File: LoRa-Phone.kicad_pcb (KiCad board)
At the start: 6 copper layers, 60 x 105 mm, 245 parts, among them IC1 W9825G6KH-6I, J1 Conn_Coaxial, J10 GPIOs, J11 Micro_SD_Card, J3 USB-C, J4 BUTTON, J5 LED0123, J6 ROTARY_ENCODER, J7 3.3V, J8 AudioJack4_Ground_SwitchTR1, J9 SWD, M1 Motor_DC, Q2 AO3400A, Q3 AO3400A, Q4 2N7002, Q6 AO3401A, SW1 SW_Push, SW2 BOOT, SW3 RESET, U1 MAX16150AUT+T, U10 DRV2605LDGS, U11 LC76G, U13 SA818S, U14 74HC138, U15 STM32H743BITx, U17 TPS61165DRV, U18 CP2102N-Axx-xQFN24, U19 ESP32-C3-WROOM-02, U2 TPS62132, U21 WM8960, U22 TLV75528PDBV, U23 E22-900M30S, U24 E22-170M30S, U3 RV-3028-C7, U4 BMP390, U5 MAX98357A, U6 LSM6DSOXTR, U7 MAX17048G_T10, U8 BQ24072RGT, U9 PLP5012PWR, Y1 Crystal_GND24

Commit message: Routed RF Core
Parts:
- removed AE4, AE5: Antenna_Shield, Connector_Coaxial:SMA_Amphenol_132289_EdgeMount
- removed BT1: Battery_Cell, Connector_JST:JST_PH_S2B-PH-K_1x02_P2.00mm_Horizontal
- removed C10, C14, C82, C84: 0.1uF, Capacitor_SMD:C_0603_1608Metric
- removed C11: 3.3nF, Capacitor_SMD:C_0603_1608Metric
- removed C12 (x2): 100nF, Capacitor_SMD:C_0805_2012Metric
- removed C13: 22uF, Capacitor_SMD:C_0805_2012Metric
- removed C15, C41, C78: 10uF, Capacitor_SMD:C_0603_1608Metric
- removed C18, C19, C30, C31, C34, C60, C63, C64, C65, C66, C68, C70: 1uF, Capacitor_SMD:C_0603_1608Metric
- removed C20, C21, C22, C43, C44, C83, C85: 4.7uF, Capacitor_SMD:C_0603_1608Metric
- removed C32, C33, C71, C72, C73, C74, C75, C76, C77, C80, C81, C86: 100nF, Capacitor_SMD:C_0603_1608Metric
- removed C35 (x2): 10uF, Capacitor_SMD:C_0805_2012Metric
- removed C42: 220nF, Capacitor_SMD:C_0603_1608Metric
- removed C45, C46, C47, C48, C49, C50, C51, C52, C53, C54, C55, C56, C57, C58, C59, C67, C69, C79: 100nF, Capacitor_SMD:C_0402_1005Metric_Pad0.74x0.62mm_HandSolder
- removed the C6 at (277.0, 45.2)
- removed the C6 at (177.9, 82.1)
- removed C61, C62: 10uF, Capacitor_SMD:C_0402_1005Metric
- removed the C7 at (277.0, 47.7)
- removed the C7 at (177.9, 84.6)
- removed C88, C94: 12pF, Capacitor_SMD:C_0402_1005Metric
- removed C9: 10uF, Capacitor_SMD:C_1210_3225Metric
- removed D1: BAT54A, Package_TO_SOT_SMD:SOT-23
- removed D3: ~, Diode_SMD:D_SOD-123
- removed FB3, FB4: FerriteBead, Inductor_SMD:L_0805_2012Metric
- removed HOLE0 (x4): MountingHole_2.2mm_M2_DIN965_Pad, MountingHole:MountingHole_2.2mm_M2_DIN965_Pad
- removed J10: GPIOs, Connector_PinHeader_2.54mm:PinHeader_2x17_P2.54mm_Vertical
- removed J11: Micro_SD_Card, PTCR:J_SD_Card-micro_socket_A
- removed J3: USB-C, Connector_USB:USB_C_Receptacle_GCT_USB4105-xx-A_16P_TopMnt_Horizontal
- removed J5: LED0123, Connector_PinHeader_1.27mm:PinHeader_2x06_P1.27mm_Vertical
- removed J7: 3.3V, Connector_PinHeader_1.27mm:PinHeader_1x01_P1.27mm_Vertical
- removed J8: AudioJack4_Ground_SwitchTR1, Connector_Audio:Jack_3.5mm_PJ31060-I_Horizontal
- removed J9: SWD, Connector_PinHeader_2.54mm:PinHeader_1x05_P2.54mm_Vertical
- removed L1: 2.2uH, Inductor_SMD:L_Coilcraft_XxL4020
- removed L3: 10uH, Inductor_SMD:L_Bourns-SRN4018
- removed LS1: Speaker, Connector_PinHeader_1.27mm:PinHeader_1x02_P1.27mm_Vertical
- removed MK1: ICS-43434, Connector_PinHeader_1.27mm:PinHeader_2x03_P1.27mm_Vertical
- removed Q2, Q3: AO3400A, Package_TO_SOT_SMD:SOT-23
- removed Q4: 2N7002, Package_TO_SOT_SMD:SOT-23
- removed Q6: AO3401A, Package_TO_SOT_SMD:SOT-23
- removed R10, R12, R13, R17, R18, R19, R59, R60, R62: 100K, Resistor_SMD:R_0603_1608Metric
- removed R14, R23, R27, R32, R35, R37, R38, R61, R63, R64, R69, R71, R72, R73, R9: 10K, Resistor_SMD:R_0603_1608Metric
- removed R20: 46.4K, Resistor_SMD:R_0603_1608Metric
- removed R21: 1.18K, Resistor_SMD:R_0603_1608Metric
- removed R22: 1.13K, Resistor_SMD:R_0603_1608Metric
- removed R25: 5K, Resistor_SMD:R_0603_1608Metric
- removed R26, R28: 1.5K, Resistor_SMD:R_0603_1608Metric
- removed R29, R30: 5.1K, Resistor_SMD:R_0603_1608Metric
- removed R31 (x2), R65 (x2), R66 (x2), R67 (x2), R68 (x2): 47K, Resistor_SMD:R_0603_1608Metric_Pad0.98x0.95mm_HandSolder
- removed R33, R34: 4.7K, Resistor_SMD:R_0603_1608Metric
- removed R36: 0.57R, Resistor_SMD:R_0603_1608Metric
- removed R39, R40, R41, R42, R43, R44, R45, R46, R47, R48, R49, R50, R51, R52, R53, R54, R55, R56, R57, R58: 22R, Resistor_SMD:R_0402_1005Metric
- removed SW1: SW_Push, Connector_PinHeader_1.27mm:PinHeader_1x02_P1.27mm_Vertical
- removed SW2: BOOT, Button_Switch_SMD:Panasonic_EVQPUJ_EVQPUA
- removed SW3: RESET, Button_Switch_SMD:Panasonic_EVQPUJ_EVQPUA
- removed TP1: +BATT, TestPoint:TestPoint_Pad_D1.0mm
- removed TP3: GND, TestPoint:TestPoint_Pad_D1.0mm
- removed TP5: CLR, TestPoint:TestPoint_Pad_D1.0mm
- removed TP6: 3V3, TestPoint:TestPoint_Pad_D1.0mm
- removed TP7: VBUS, TestPoint:TestPoint_Pad_D1.0mm
- removed TP8: CHG, TestPoint:TestPoint_Pad_D1.0mm
- removed TP9: VCC, TestPoint:TestPoint_Pad_D1.0mm
- removed U14: 74HC138, PTCR:SO-16
- removed U15: STM32H743BITx, Package_QFP:LQFP-208_28x28mm_P0.5mm
- removed U16: ~, Connector_FFC-FPC:TE_4-1734839-0_1x40-1MP_P0.5mm_Horizontal
- removed U17: TPS61165DRV, Package_SON:WSON-6-1EP_2x2mm_P0.65mm_EP1x1.6mm
- removed U18: CP2102N-Axx-xQFN24, Package_DFN_QFN:QFN-24-1EP_4x4mm_P0.5mm_EP2.6x2.6mm
- removed U19: ESP32-C3-WROOM-02, RF_Module:ESP32-C3-WROOM-02U
- removed U20: ~, Connector_FFC-FPC:TE_2-1734839-4_1x24-1MP_P0.5mm_Horizontal
- removed U22: TLV75528PDBV, Package_TO_SOT_SMD:SOT-23-5
- removed U5: MAX98357A, PTCR:QFN50P300X300X100-17N-D
- removed U7: MAX17048G_T10, PTCR:SON50P200X200X80-9N-R100X170
- removed U8: BQ24072RGT, PTCR:QFN50P300X300X100-17N-D
- removed U9: PLP5012PWR, PTCR:TSSOP24_PW_TEX
- removed Y1: Crystal_GND24, Crystal:Crystal_SMD_Abracon_ABM8AIG-4Pin_3.2x2.5mm
- added C100: 100pF, Capacitor_SMD:C_0603_1608Metric, F.Cu at (383.2, 65.6)
- added C101: 1nF, Capacitor_SMD:C_0402_1005Metric, F.Cu at (173.2, 64.9)
- added C102: 1nF, Capacitor_SMD:C_0402_1005Metric, F.Cu at (172.7, 60.9)
- added C103: 1nF, Capacitor_SMD:C_0402_1005Metric, F.Cu at (191.0, 76.9)
- added C104: 100pF, Capacitor_SMD:C_0603_1608Metric, F.Cu at (383.2, 75.7)
- added C105: 0.1uF, Capacitor_SMD:C_0603_1608Metric, F.Cu at (383.2, 78.2)
- added C106: 100pF, Capacitor_SMD:C_0603_1608Metric, F.Cu at (383.2, 80.7)
- added C107: 0.1uF, Capacitor_SMD:C_0603_1608Metric, F.Cu at (383.2, 83.2)
- added C108: 1nF, Capacitor_SMD:C_0603_1608Metric, F.Cu at (387.2, 63.1)
- added C109: 100pF, Capacitor_SMD:C_0603_1608Metric, F.Cu at (387.2, 65.6)
- added C110: 0.1uF, Capacitor_SMD:C_0603_1608Metric, F.Cu at (387.2, 68.1)
- added C111: 1nF, Capacitor_SMD:C_0603_1608Metric, F.Cu at (387.2, 70.7)
- added C112: 1nF, Capacitor_SMD:C_0402_1005Metric, F.Cu at (387.2, 73.2)
- added C113: 100pF, Capacitor_SMD:C_0603_1608Metric, F.Cu at (387.2, 75.7)
- added C114: 0.1uF, Capacitor_SMD:C_0603_1608Metric, F.Cu at (387.2, 78.2)
- added C6: 100nF, Capacitor_SMD:C_0603_1608Metric, F.Cu at (371.1, 68.1)
- added C7: 10uF, Capacitor_SMD:C_0603_1608Metric, F.Cu at (371.1, 70.7)
- added C99: 100pF, Capacitor_SMD:C_0603_1608Metric, F.Cu at (383.2, 63.1)
- added IC2: AD8318ACPZ-REEL7, PTCR:QFN65P400X400X100-17N, F.Cu at (184.3, 57.3)
- added IC3: AD8318ACPZ-REEL7, PTCR:QFN65P400X400X100-17N, F.Cu at (183.1, 67.0)
- added MH0: MountingHole_2.2mm_M2_DIN965_Pad_TopBottom, MountingHole:MountingHole_2.2mm_M2_DIN965_Pad_TopBottom, F.Cu at (171.6, 56.5)
- added MH0: MountingHole_2.2mm_M2_DIN965_Pad_TopBottom, MountingHole:MountingHole_2.2mm_M2_DIN965_Pad_TopBottom, F.Cu at (121.6, 56.5)
- added MH0: MountingHole_2.2mm_M2_DIN965_Pad_TopBottom, MountingHole:MountingHole_2.2mm_M2_DIN965_Pad_TopBottom, F.Cu at (121.6, 148.5)
- added R84: 96.2R, Resistor_SMD:R_0402_1005Metric, F.Cu at (137.3, 64.5)
- added R85: 71.5R, Resistor_SMD:R_0402_1005Metric, F.Cu at (135.5, 64.0)
- added R86: 96.2R, Resistor_SMD:R_0402_1005Metric, F.Cu at (133.9, 60.3)
- added R87: 96.2R, Resistor_SMD:R_0402_1005Metric, F.Cu at (137.3, 60.3)
- added R88: 71.5R, Resistor_SMD:R_0402_1005Metric, F.Cu at (135.5, 60.8)
- added R89: 52.3R, Resistor_SMD:R_0402_1005Metric, F.Cu at (392.4, 129.6)
- added R90: 499R, Resistor_SMD:R_0402_1005Metric, F.Cu at (392.4, 131.6)
- added R91: 10K, Resistor_SMD:R_0402_1005Metric, F.Cu at (392.4, 133.6)
- added R92: 10K, Resistor_SMD:R_0402_1005Metric, F.Cu at (392.4, 135.5)
- added R93: 52.3R, Resistor_SMD:R_0402_1005Metric, F.Cu at (395.3, 127.6)
- added R94: 499R, Resistor_SMD:R_0402_1005Metric, F.Cu at (395.3, 129.6)
- added R95: 10K, Resistor_SMD:R_0603_1608Metric, F.Cu at (391.2, 83.2)
- added R96: 1K, Resistor_SMD:R_0402_1005Metric, F.Cu at (395.3, 131.6)
- added R97: 1K, Resistor_SMD:R_0402_1005Metric, F.Cu at (395.3, 133.6)
- AE1: value Antenna_Shield -> GNSS
- AE6: value Antenna_Shield -> SMA; moved to F.Cu
- IC1: value W9825G6KH-6I -> SKY13373-460LF; footprint PTCR:SOP80P1176X120-54N -> PTCR:QFN50P200X200X60-13N-D
- J1: value Conn_Coaxial -> Interface; footprint Connector_Coaxial:U.FL_Molex_MCRF_73412-0110_Vertical -> Connector_PinHeader_2.54mm:PinHeader_2x20_P2.54mm_Vertical; moved to B.Cu
- R83: value 1M -> 96.2R
- U1: value MAX16150AUT+T -> ESP32-S3-WROOM-2; footprint PTCR:21-0058I_MXM -> RF_Module:ESP32-S3-WROOM-2
- U11, U23: moved to F.Cu
- U2: value TPS62132 -> TCD-10-23BDX+; footprint PTCR:RGT16_1P7X1P7 -> PTCR:TCD-10-23BDX+
- U3: value RV-3028-C7 -> MCP23017x-x-ML; footprint Package_SON:MicroCrystal_C7_SON-8_1.5x3.2mm_P0.9mm -> Package_DFN_QFN:QFN-28-1EP_6x6mm_P0.65mm_EP4.25x4.25mm
- moved U21 245.2 mm to (391.4, 140.0)
- moved C40 203.9 mm to (379.1, 63.1)
- moved C95 202.6 mm to (379.1, 80.7)
- moved C96 202.6 mm to (379.1, 83.2)
- moved C23 196.7 mm to (371.1, 80.7)
- moved C36 195.4 mm to (375.1, 75.7)
- moved C37 195.4 mm to (375.1, 78.2)
- moved C38 195.4 mm to (375.1, 80.7)
- moved C39 195.4 mm to (375.1, 83.2)
- moved C16 194.7 mm to (371.1, 75.7)
- moved C17 194.7 mm to (371.1, 78.2)
- moved C25 193.9 mm to (375.1, 63.1)
- moved C26 193.9 mm to (375.1, 65.6)
- moved C27 193.9 mm to (375.1, 68.1)
- moved C28 193.9 mm to (375.1, 70.7)
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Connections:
- AE6 pad 1: Net-(AE6-A) -> ANT
- C25 pad 1: NRST_900 -> NRST_RADIO
- C28 pad 1: NRST_170 -> NRST_RADIO
- C4 pad 2: +2V8 -> +3V3
- C8 pad 1: CLR_POWER -> +3V3
- IC1 pad 1: +3V3 -> RF1
- IC1 pad 10: DQ5 -> GND
- IC1 pad 11: DQ6 -> ROS
- IC1 pad 13: DQ7 -> GND
- IC1 pad 2: DQ0 -> GND
- IC1 pad 3: +3V3 -> RF3
- IC1 pad 4: DQ1 -> RFS_V1
- IC1 pad 5: DQ2 -> RFS_V2
- IC1 pad 6: GND -> +3V3
- IC1 pad 7: DQ3 -> GND
- IC1 pad 8: DQ4 -> GND
- IC1 pad 9: +3V3 -> RF2
- J1 pad 1: unconnected-(J1-In-Pad1) -> +5V
- J1 pad 2: GND -> +3V3
- R81 pad 2: Net-(U15-PA2) -> Net-(U1-IO38)
- R82 pad 2: Net-(U15-PA3) -> Net-(U1-MTCK/IO39)
- R83 pad 1: XTAL2 -> FWD_IN
- R83 pad 2: XTAL1 -> GND
- U1 pad 1: Net-(U1-*PB_IN) -> GND
- U1 pad 2: GND -> +3V3
- U1 pad 3: VCC -> S3_EN
- U1 pad 4: EN_POWER -> FWD
- U1 pad 5: unconnected-(U1-*INT-Pad5) -> BUSY_170
- U1 pad 6: CLR_POWER -> DIO1_900
- U11 pad 4: 1PPS -> unconnected-(U11-1PPS-Pad4)
- U13 pad 12: Net-(AE5-A) -> RF1
- U2 pad 1: Net-(L1-Pad2) -> FWD_IN
- U2 pad 2: Net-(L1-Pad2) -> GND
- U2 pad 3: Net-(L1-Pad2) -> ROS
- U2 pad 4: Net-(U2-PG) -> ANT
- U2 pad 6: GND -> REV_IN
- U21 pad 17: WM8960_SCL -> SCL
- U21 pad 18: WM8960_SDA -> SDA
- U23 pad 15: NRST_900 -> NRST_RADIO
- U23 pad 21: Net-(AE6-A) -> RF2
- U23 pad 7: TXEN_900 -> Net-(U23-DIO2)
- U23 pad 8: DIO2_900 -> Net-(U23-DIO2)
- U24 pad 15: NRST_170 -> NRST_RADIO
- U24 pad 21: Net-(AE4-A) -> RF3
- U24 pad 7: TXEN_170 -> Net-(U24-DIO2)
- U24 pad 8: DIO2_170 -> Net-(U24-DIO2)
- U3 pad 1: unconnected-(U3-CLKOUT-Pad1) -> MOTOR
- U3 pad 2: INT_RTC -> RXEN_170
- U3 pad 3: SCL -> NRST_RADIO
- U3 pad 4: SDA -> RXEN_900
- U3 pad 5: GND -> +3V3
- U3 pad 6: +BATT -> GND
- U3 pad 7: +3V3 -> unconnected-(U3-NC-Pad7)
- U3 pad 8: unconnected-(U3-EVI-Pad8) -> SCL
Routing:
- net A10: track 57.9 -> 0.00 mm, vias 2 -> 0
- net ~CS: track 49.9 -> 0.00 mm, vias 2 -> 0
- net A11: track 48.7 -> 0.00 mm, vias 2 -> 0
- net Net-(C45-Pad1): track 46.6 -> 0.00 mm
- net A9: track 45.8 -> 0.00 mm, vias 2 -> 0
- net A8: track 44.7 -> 0.00 mm, vias 2 -> 0
- net CKE: track 44.5 -> 0.00 mm, vias 2 -> 0
- net A5: track 44.0 -> 0.00 mm
- net A7: track 43.4 -> 0.00 mm, vias 2 -> 0
- net A6: track 43.1 -> 0.00 mm, vias 2 -> 0
- net A4: track 42.7 -> 0.00 mm
- net A3: track 40.9 -> 0.00 mm, vias 2 -> 0
- net A2: track 40.9 -> 0.00 mm, vias 2 -> 0
- net A12: track 40.4 -> 0.00 mm, vias 2 -> 0
- net A1: track 40.2 -> 0.00 mm, vias 2 -> 0
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- added copper zone on F.Cu, net RF2
- added copper zone on F.Cu, net RF3
- added copper zone on F.Cu, net ROS
- removed copper zone on F.Cu, net +3V3
- removed copper zone on F.Cu, net +BATT
- removed copper zone on In3.Cu, net GND
- removed copper zone on In4.Cu, net GND
- removed copper zone on B.Cu, net VBUS
- removed copper zone on F.Cu, net VBUS
- removed copper zone on F.Cu, net VCC
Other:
- board size 60 x 105 mm -> 60 x 102.5 mm
- copper layers 6 -> 4

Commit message: Routed RF part and started routing MCU, SPI Bus, and other
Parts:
- removed C17, C36: 4.7uF, Capacitor_SMD:C_0603_1608Metric
- removed R91: 10K, Resistor_SMD:R_0402_1005Metric
- added REF**: antipad, PTCR:antipad, F.Cu at (122.5, 70.1)
- C104, C105, C106, C107, C108, C109, C110, C111, C113, C114: footprint Capacitor_SMD:C_0603_1608Metric -> Capacitor_SMD:C_0402_1005Metric
- moved C37 308.6 mm to (66.7, 68.9)
- moved R74 308.6 mm to (78.7, 74.0)
- moved R75 308.6 mm to (82.7, 53.9)
- moved R76 308.6 mm to (82.7, 56.4)
- moved R77 308.6 mm to (82.7, 58.9)
- moved C87 308.6 mm to (70.7, 56.4)
- moved C89 308.6 mm to (70.7, 58.9)
- moved C90 308.6 mm to (70.7, 61.4)
- moved C92 308.6 mm to (70.7, 66.4)
- moved C93 308.6 mm to (70.7, 68.9)
- moved R93 262.2 mm to (142.9, 56.5), turned to -90 degrees
- moved R89 257.6 mm to (142.5, 66.9), turned to 90 degrees
- moved R94 257.4 mm to (149.2, 54.1), turned to 90 degrees
- moved R97 254.0 mm to (152.7, 58.0), turned to 180 degrees
- moved R90 252.8 mm to (148.8, 63.7), turned to 90 degrees
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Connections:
- C16 pad 1: Net-(U21-AVDD) -> +3V3
- C38 pad 1: Net-(U21-DCVDD) -> +3V3
- U21 pad 21: Net-(U21-SPKVDD2) -> unconnected-(U21-SPKVDD2-Pad21)
- U21 pad 26: Net-(U21-SPKVDD1) -> unconnected-(U21-SPKVDD1-Pad26)
- U21 pad 32: Net-(U21-AVDD) -> +3V3
- U21 pad 8: Net-(U21-DCVDD) -> +3V3
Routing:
- net MOSI: track 0.00 -> 124.2 mm, vias 0 -> 6
- net CLK: track 0.00 -> 119.4 mm, vias 0 -> 6
- net MISO: track 0.00 -> 117.2 mm, vias 0 -> 4
- net +3V3: track 0.00 -> 96.7 mm, vias 0 -> 6
- net FWD: track 0.00 -> 96.5 mm, vias 0 -> 2
- net DIO1_900: track 0.00 -> 94.6 mm, vias 0 -> 4
- net CS_900: track 0.00 -> 88.3 mm, vias 0 -> 4
- net REV: track 0.00 -> 82.8 mm, vias 0 -> 2
- net PTT: track 0.00 -> 79.9 mm, vias 0 -> 5
- net BUSY_900: track 0.00 -> 75.6 mm, vias 0 -> 4
- net NRST_RADIO: track 0.00 -> 69.1 mm, vias 0 -> 3
- net CS_170: track 0.00 -> 59.1 mm, vias 0 -> 3
- net BUSY_170: track 0.99 -> 58.1 mm, vias 0 -> 2
- net H/L: track 0.00 -> 56.0 mm, vias 0 -> 3
- net MONO_OUT: track 0.00 -> 52.2 mm, vias 0 -> 1
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- added copper zone on F.Cu, net +3V3
- added copper zone on In2.Cu, net +3V3
- added copper zone on F.Cu, net RF1
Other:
- outline, holes or cut-outs redrawn

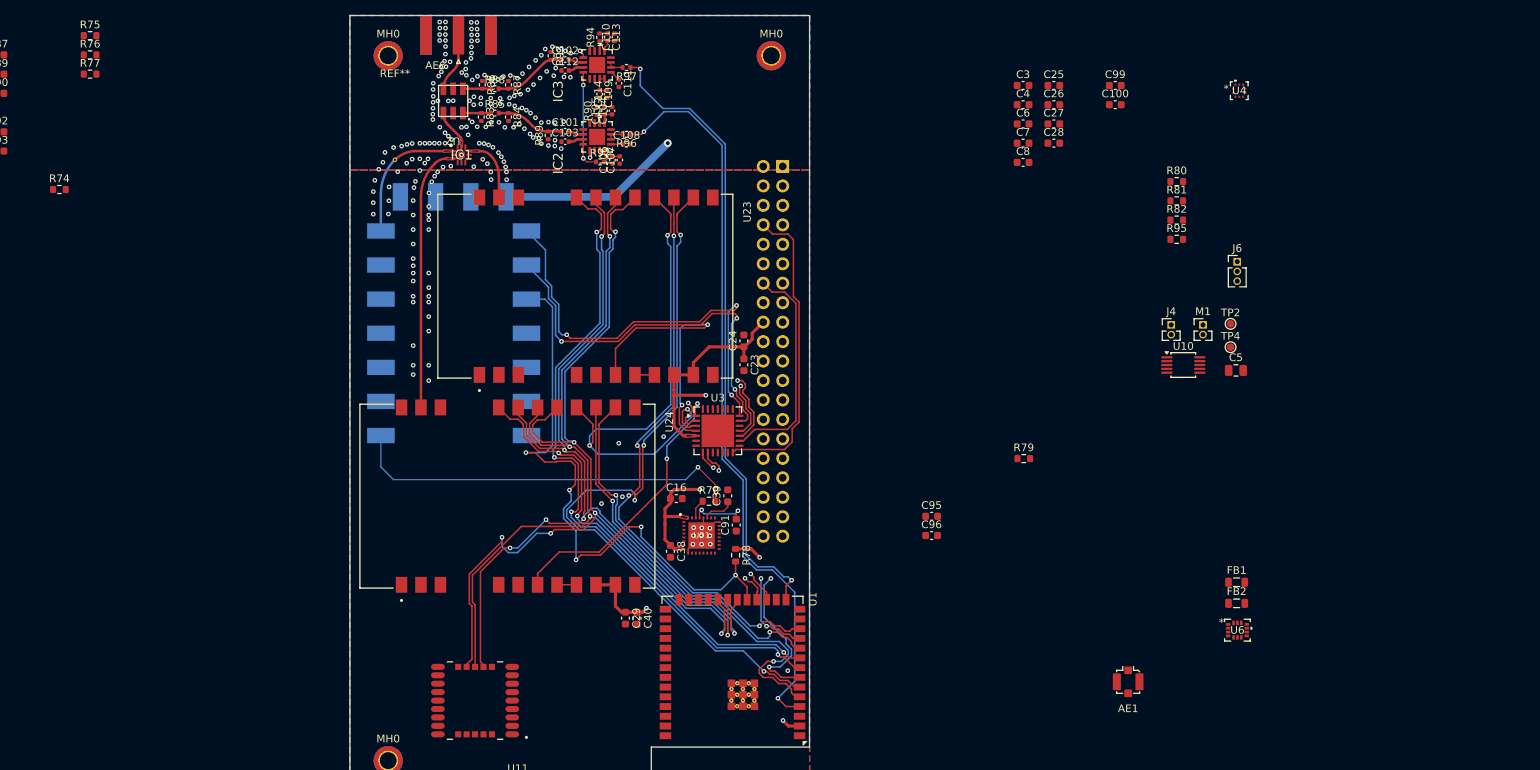
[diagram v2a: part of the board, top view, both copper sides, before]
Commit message: Modified schematic to add dual battery with dual charger, dual gauge and power mux
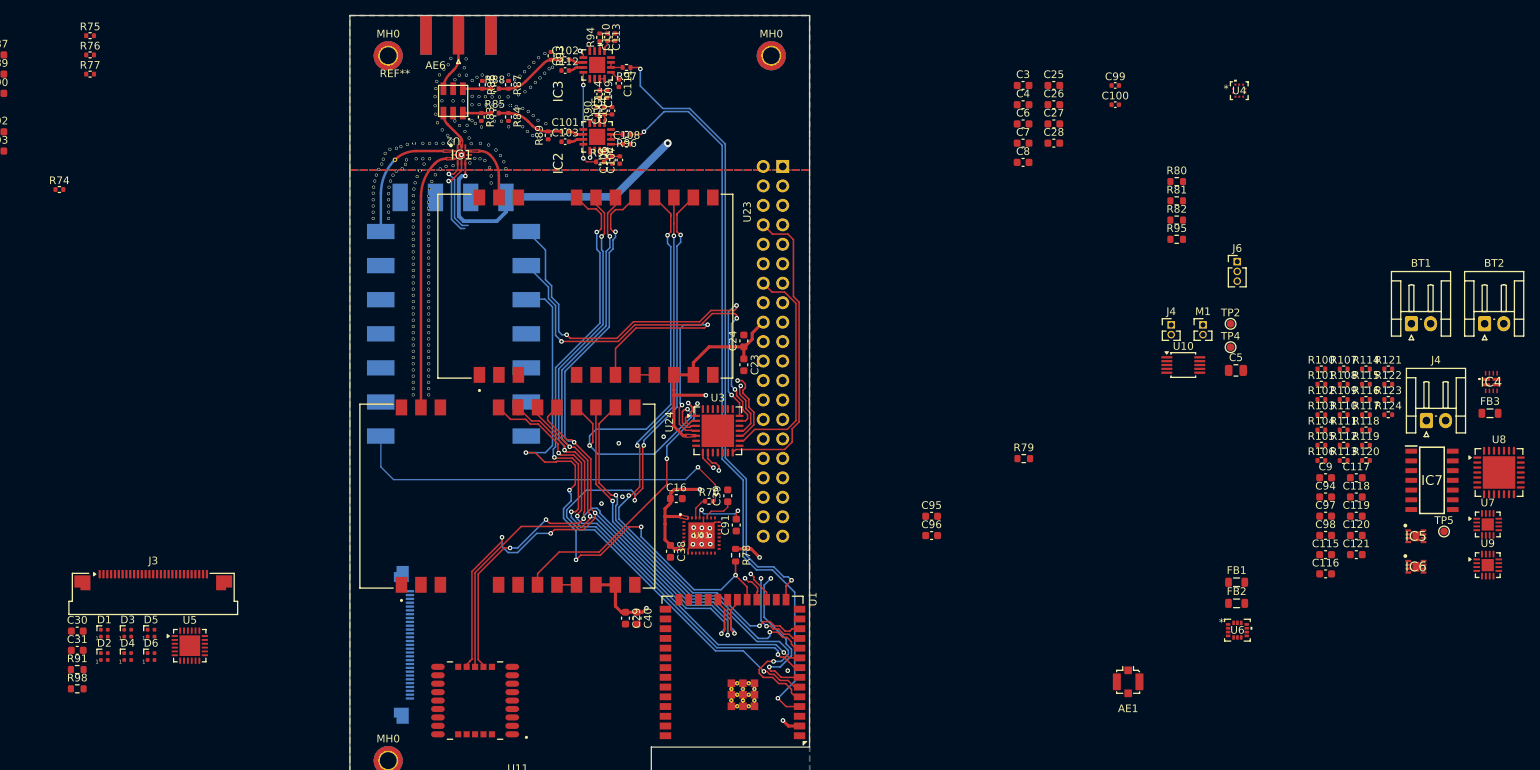
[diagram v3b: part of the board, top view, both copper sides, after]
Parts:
- added BT1: MAIN, Connector_JST:JST_EH_S2B-EH_1x02_P2.50mm_Horizontal, F.Cu at (255.2, 91.5)
- added BT2: SECOND, Connector_JST:JST_EH_S2B-EH_1x02_P2.50mm_Horizontal, F.Cu at (264.7, 91.5)
- added C115: 4.7uF, Capacitor_SMD:C_0603_1608Metric, F.Cu at (243.9, 121.6)
- added C116: 1uF, Capacitor_SMD:C_0603_1608Metric, F.Cu at (243.9, 124.1)
- added C117: 1uF, Capacitor_SMD:C_0603_1608Metric, F.Cu at (248.0, 111.6)
- added C118: 1uF, Capacitor_SMD:C_0603_1608Metric, F.Cu at (248.0, 114.1)
- added C119: 4.7uF, Capacitor_SMD:C_0603_1608Metric, F.Cu at (248.0, 116.6)
- added C120: 4.7uF, Capacitor_SMD:C_0603_1608Metric, F.Cu at (248.0, 119.1)
- added C121: 100nF, Capacitor_SMD:C_0603_1608Metric, F.Cu at (248.0, 121.6)
- added C30: 1uF, Capacitor_SMD:C_0603_1608Metric, F.Cu at (81.0, 131.6)
- added C31: 0.1uF, Capacitor_SMD:C_0603_1608Metric, F.Cu at (81.0, 134.1)
- added C9: 100nF, Capacitor_SMD:C_0603_1608Metric, F.Cu at (243.9, 111.6)
- added C94: 0.1uF, Capacitor_SMD:C_0603_1608Metric, F.Cu at (243.9, 114.1)
- added C97: 4.7uF, Capacitor_SMD:C_0603_1608Metric, F.Cu at (243.9, 116.6)
- added C98: 1uF, Capacitor_SMD:C_0603_1608Metric, F.Cu at (243.9, 119.1)
- added D1: LED_ARBG, LED_SMD:LED_SK6812_EC15_1.5x1.5mm, F.Cu at (84.5, 131.9)
- added D2: LED_ARBG, LED_SMD:LED_SK6812_EC15_1.5x1.5mm, F.Cu at (84.5, 134.9)
- added D3: LED_ARBG, LED_SMD:LED_SK6812_EC15_1.5x1.5mm, F.Cu at (87.6, 131.9)
- added D4: LED_ARBG, LED_SMD:LED_SK6812_EC15_1.5x1.5mm, F.Cu at (87.6, 134.9)
- added D5: LED_ARBG, LED_SMD:LED_SK6812_EC15_1.5x1.5mm, F.Cu at (90.7, 131.9)
- added D6: LED_ARBG, LED_SMD:LED_SK6812_EC15_1.5x1.5mm, F.Cu at (90.7, 134.9)
- added FB3: FerriteBead, Inductor_SMD:L_0805_2012Metric, F.Cu at (265.4, 103.2)
- added IC4: TPS2121RUXT, PTCR:TPS2121RUXT, F.Cu at (265.6, 99.1)
- added IC5: MAX17048G+T10, PTCR:SON50P200X200X80-9N-D, F.Cu at (255.7, 119.2)
- added IC6: MAX17048G+T10, PTCR:SON50P200X200X80-9N-D, F.Cu at (255.7, 123.2)
- added IC7: TCA9543ADR, PTCR:SOIC127P600X175-14N, F.Cu at (257.8, 111.9)
- added J2: Connector, Connector_FFC-FPC:Amphenol_F32R-1A7x1-11029_1x29-1MP_P0.5mm_Horizontal, B.Cu at (121.5, 133.4)
- added J3: Connector, Connector_FFC-FPC:Amphenol_F32R-1A7x1-11029_1x29-1MP_P0.5mm_Horizontal, F.Cu at (90.9, 127.1)
- added J4: JST_MAIN, Connector_JST:JST_EH_S2B-EH_1x02_P2.50mm_Horizontal, F.Cu at (257.1, 104.1)
- added R100: 13.7K, Resistor_SMD:R_0402_1005Metric, F.Cu at (243.4, 97.4)
- added R101: 23.7K, Resistor_SMD:R_0402_1005Metric, F.Cu at (243.4, 99.4)
- added R102: 5K, Resistor_SMD:R_0402_1005Metric, F.Cu at (243.4, 101.4)
- added R103: 5K, Resistor_SMD:R_0402_1005Metric, F.Cu at (243.4, 103.4)
- added R104: 51.1K, Resistor_SMD:R_0402_1005Metric, F.Cu at (243.4, 105.3)
- added R105: 10.2K, Resistor_SMD:R_0402_1005Metric, F.Cu at (243.4, 107.3)
- added R106: 5K, Resistor_SMD:R_0402_1005Metric, F.Cu at (243.4, 109.3)
- added R107: 1K, Resistor_SMD:R_0402_1005Metric, F.Cu at (246.3, 97.4)
- added R108: 1K, Resistor_SMD:R_0402_1005Metric, F.Cu at (246.3, 99.4)
- added R109: 10K, Resistor_SMD:R_0402_1005Metric, F.Cu at (246.3, 101.4)
- added R110: 1.13K, Resistor_SMD:R_0402_1005Metric, F.Cu at (246.3, 103.4)
- added R111: 1.18K, Resistor_SMD:R_0402_1005Metric, F.Cu at (246.3, 105.3)
- added R112: 1.18K, Resistor_SMD:R_0402_1005Metric, F.Cu at (246.3, 107.3)
- added R113: 1.13K, Resistor_SMD:R_0402_1005Metric, F.Cu at (246.3, 109.3)
- added R114: 1K, Resistor_SMD:R_0402_1005Metric, F.Cu at (249.2, 97.4)
- added R115: 1K, Resistor_SMD:R_0402_1005Metric, F.Cu at (249.2, 99.4)
- added R116: 10K, Resistor_SMD:R_0402_1005Metric, F.Cu at (249.2, 101.4)
- added R117: 10K, Resistor_SMD:R_0402_1005Metric, F.Cu at (249.2, 103.4)
- added R118: 10K, Resistor_SMD:R_0402_1005Metric, F.Cu at (249.2, 105.3)
- added R119: 10K, Resistor_SMD:R_0402_1005Metric, F.Cu at (249.2, 107.3)
- added R120: 10K, Resistor_SMD:R_0402_1005Metric, F.Cu at (249.2, 109.3)
- added R121: 10K, Resistor_SMD:R_0402_1005Metric, F.Cu at (252.1, 97.4)
- added R122: 10K, Resistor_SMD:R_0402_1005Metric, F.Cu at (252.1, 99.4)
- added R123: 10K, Resistor_SMD:R_0402_1005Metric, F.Cu at (252.1, 101.4)
- added R124: 10K, Resistor_SMD:R_0402_1005Metric, F.Cu at (252.1, 103.4)
- added R91: 3.3K, Resistor_SMD:R_0603_1608Metric, F.Cu at (81.0, 136.6)
- added R98: 10K, Resistor_SMD:R_0603_1608Metric, F.Cu at (81.0, 139.1)
- added TP5: +3V3_RF, TestPoint:TestPoint_Pad_D1.0mm, F.Cu at (259.4, 118.6)
- added U5: IS31FL3218-QF, Package_DFN_QFN:QFN-24-1EP_4x4mm_P0.5mm_EP2.7x2.7mm, F.Cu at (95.7, 133.5)
- added U7: BQ24075RGT, Package_DFN_QFN:VQFN-16-1EP_3x3mm_P0.5mm_EP1.6x1.6mm, F.Cu at (265.1, 117.7)
- added U8: MCP23017x-x-ML, Package_DFN_QFN:QFN-28-1EP_6x6mm_P0.65mm_EP4.25x4.25mm, F.Cu at (266.6, 110.9)
- added U9: BQ24075RGT, Package_DFN_QFN:VQFN-16-1EP_3x3mm_P0.5mm_EP1.6x1.6mm, F.Cu at (265.1, 123.0)
- C100, C99: footprint Capacitor_SMD:C_0603_1608Metric -> Capacitor_SMD:C_0402_1005Metric
- R70, R74, R75, R76, R77: footprint Resistor_SMD:R_0603_1608Metric -> Resistor_SMD:R_0402_1005Metric
- moved U13 0.07 mm to (130.1, 92.8)
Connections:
- C104 pad 1: +3V3 -> +3V3_RF
- C105 pad 1: +3V3 -> +3V3_RF
- C106 pad 2: +3V3 -> +3V3_RF
- C107 pad 2: +3V3 -> +3V3_RF
- C109 pad 1: +3V3 -> +3V3_RF
- C110 pad 1: +3V3 -> +3V3_RF
- C113 pad 2: +3V3 -> +3V3_RF
- C114 pad 2: +3V3 -> +3V3_RF
- C26 pad 2: +BATT -> +3V3
- IC1 pad 6: +3V3 -> +3V3_RF
- IC2 pad 3: +3V3 -> +3V3_RF
- IC2 pad 4: +3V3 -> +3V3_RF
- IC2 pad 9: +3V3 -> +3V3_RF
- IC3 pad 3: +3V3 -> +3V3_RF
- IC3 pad 4: +3V3 -> +3V3_RF
- IC3 pad 9: +3V3 -> +3V3_RF
- J1 pad 11: unconnected-(J1-Pin_11-Pad11) -> INTA_MCP_2
- J1 pad 14: INTA_MCP -> INTA_MCP_1
- R92 pad 2: +3V3 -> +3V3_RF
- U10 pad 10: +BATT -> +3V3
- U3 pad 19: unconnected-(U3-GPA2-Pad19) -> SDB
- U3 pad 22: unconnected-(U3-GPA5-Pad22) -> RFS_V2
- U3 pad 23: unconnected-(U3-GPA6-Pad23) -> RFS_V1
- U3 pad 28: unconnected-(U3-GPB3-Pad28) -> AD8318_EN
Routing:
- net +3V3_RF: track 0.00 -> 12.1 mm
- net RFS_V2: track 0.00 -> 10.8 mm, vias 0 -> 1
- net RFS_V1: track 0.00 -> 10.6 mm, vias 0 -> 1
- net MOSI: track 124.2 -> 119.7 mm
- net +3V3: track 96.7 -> 101.1 mm, vias 6 -> 7
- net MISO: track 117.2 -> 113.9 mm
- net CS_170: track 59.1 -> 58.5 mm
- net GND: vias 203 -> 226
